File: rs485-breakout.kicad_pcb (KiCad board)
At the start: 2 copper layers, 32.2 x 60.5 mm, 33 parts, among them IC1 ATTINY441-SSU, J1 Conn_01x08, J2 RJ45, J3 Conn_01x08, J4 Conn_01x08, P1 CONN_02X03, Q1 Q_PMOS_GSD, U1 SN65HVD72, U2 MCP1702, X1 16MHz

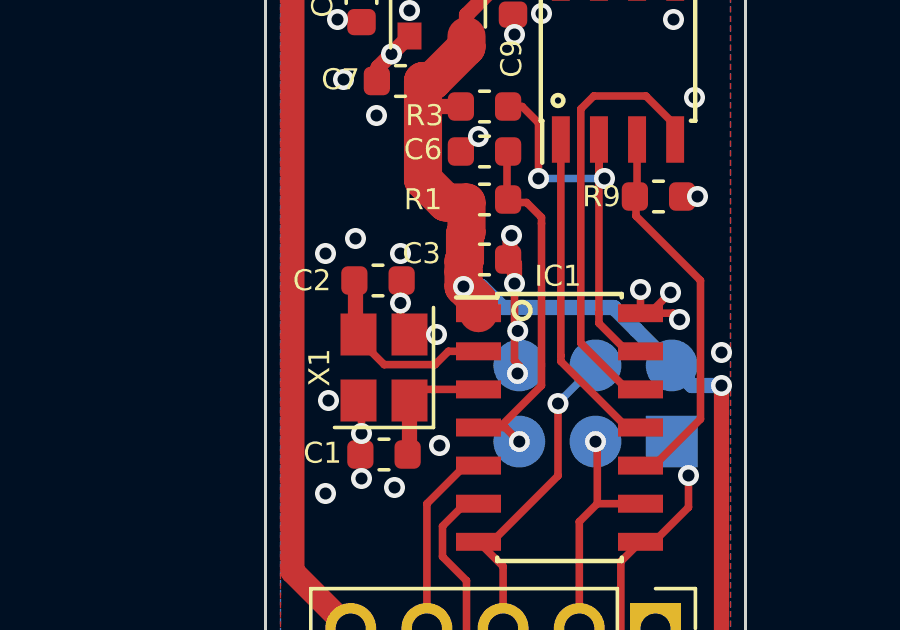
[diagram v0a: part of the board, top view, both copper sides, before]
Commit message: fix programming header silkscreen
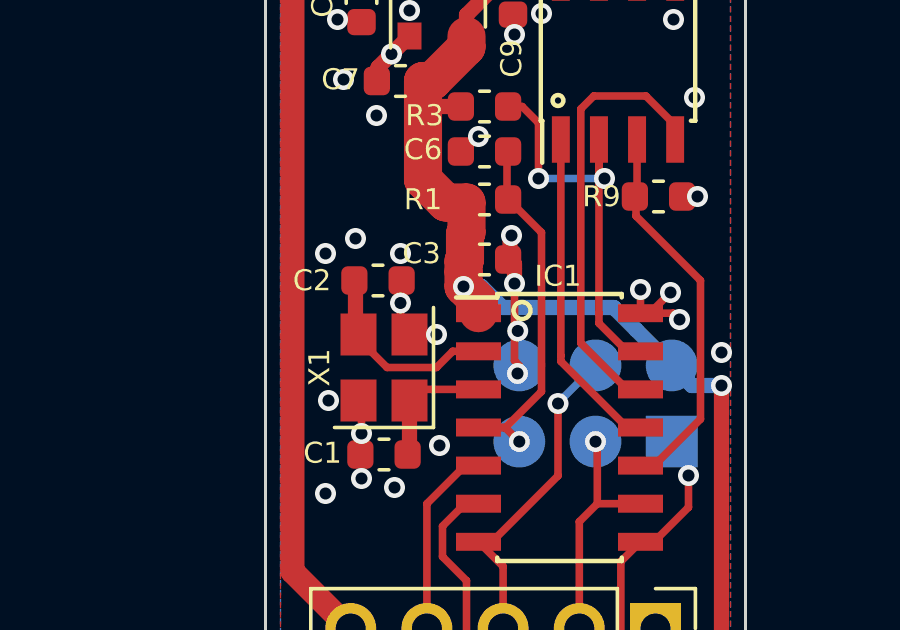
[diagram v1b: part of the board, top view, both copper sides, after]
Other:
- net class Default removed
- net class excitation removed
- net class sensor removed
- board text added: "MISO SCK RESET"
- board text removed: "RESET SCK MISO"
